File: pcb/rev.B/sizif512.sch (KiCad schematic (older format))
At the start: 216 parts, among them J1 DS1020-05, J10 DB9-M, J11 Conn_02x05_Odd_Even, J12 Mini-DIN-9, J13 RCJ-014, J14 PJ-313, J15 PJ-313, J16 Conn_02x28_Row_Letter_First, J17 Conn_01x10, J18 MEM2055-00-190-01-A, J2 DS1020-08, J3 DS-210, J4 WF-4, J5 JTAG, J6 Conn_01x02, J7 Conn_02x05_Top_Bottom, J8 Conn_01x02, J9 Conn_02x17_Odd_Even, Q1 BC547B, Q2 BC547C, Q3 BC547C, Q4 BC547C, Q5 BC547C, SW1 Conn_01x02, SW2 WF-2, SW3 WF-2, U1 74HCU04, U10 MB8877A, U11 EPM3256ATC144-10, U12 AS6C4008-55PCN, U13 74HCT4053D, U14 AY-3-8310, U15 AD724, U16 74HC245, U17 74HC245, U2 74HCT05, U3 74HCU04, U4 Z84C0010PEC, U5 L4940V5 / K7805-2000R3L, U6 AM1S-0512SZ, U7 AMS1117-3.3, U8 LM2596T-ADJ, U9 SST39SF040, Y1 17.734475 MHz, Y2 14 MHz

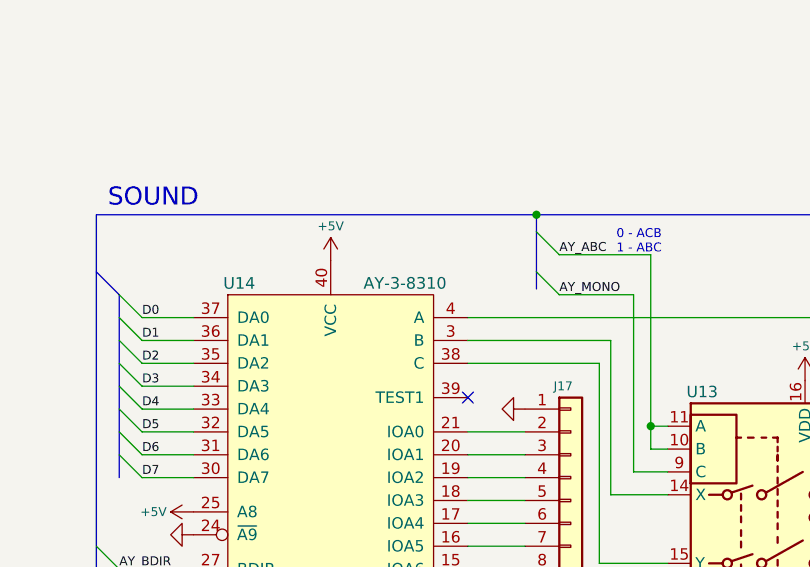
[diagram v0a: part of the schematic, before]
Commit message: add rev.B (abandoned) and rev.C (wip) pcbs
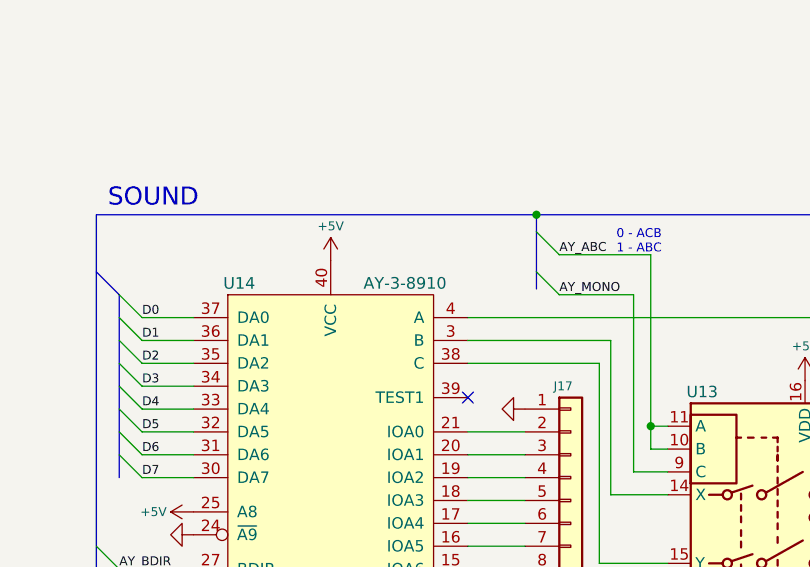
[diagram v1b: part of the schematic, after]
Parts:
- U14: value AY-3-8310 -> AY-3-8910
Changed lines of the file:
@@
 P 13800 14125
 F 0 "U14" H 13400 15425 51  0000 C CNN
-F 1 "AY-3-8310" H 14125 15425 51  0000 C CNN
+F 1 "AY-3-8910" H 14125 15425 51  0000 C CNN
 F 2 "Package_DIP:DIP-40_W15.24mm_Socket" H 13800 15725 39  0001 C CNN
 F 3 "" H 13800 15725 39  0001 C CNN
